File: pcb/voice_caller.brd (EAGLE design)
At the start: 22 parts, among them IC1 PRO_MICRO, IC2 AT45DB321D-S, IC3 78L12SMD, K4 G6J-2P-Y

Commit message: All but switches
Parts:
- added C7: (no value), rcl:C1206K
- moved C2 36.8 mm to (15.8, 39.8), turned to 0 degrees
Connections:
- net +3V3: now also C7.1
- net GND: now also C7.2
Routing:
- net GND: track 160.9 -> 164.2 mm
- net +5V: track 26.8 -> 29.9 mm
- net +3V3: track 10.2 -> 11.7 mm
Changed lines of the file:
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@@
 <elements>
 <element name="C1" library="rcl" package="C1206K" value="" x="37.823125" y="56.125625" rot="R180"/>
-<element name="C2" library="rcl" package="C1206K" value="" x="51.579403125" y="30.948178125" rot="R270"/>
+<element name="C2" library="rcl" package="C1206K" value="" x="15.803696875" y="39.752528125"/>
 <element name="IC2" library="memory-atmel" package="SO08-8S2" value="AT45DB321D-S" x="27.18" y="35.015" rot="R90"/>
 <element name="CONN_MIC" library="con-tycoelectronics" package="RJ45-NO-SHIELD" value="RJ45-8L-B" x="16.19" y="55.19" rot="R270">
@@
 <element name="R6" library="rcl" package="M1206" value="" x="36.37" y="9.68375" rot="R270"/>
 <element name="R7" library="rcl" package="M1206" value="1k" x="33.3375" y="23.65375" rot="R180"/>
+<element name="C7" library="rcl" package="C1206K" value="" x="19.446875" y="35.004375" rot="R270"/>
 </elements>
 <signals>
@@
 <wire x1="30.6775" y1="52.22875" x2="30.8375" y2="52.38875" width="0.3048" layer="1"/>
 <contactref element="K4" pad="1"/>
-<wire x1="35.123125" y1="52.79" x2="51.579403125" y2="32.448178125" width="0" layer="19" extent="1-1"/>
-<wire x1="29.781375" y1="16.66280625" x2="51.579403125" y2="32.448178125" width="0" layer="19" extent="1-1"/>
+<wire x1="14.303696875" y1="39.752528125" x2="14.5" y2="39.752528125" width="0.4064" layer="1"/>
+<wire x1="14.5" y1="39.752528125" x2="14.5" y2="42.62" width="0.4064" layer="1"/>
+<wire x1="29.781375" y1="16.66280625" x2="14.5" y2="39.752528125" width="0" layer="19" extent="1-1"/>
 </signal>
 <signal name="GND">
@@
 <wire x1="45.4025" y1="25.003125" x2="45.4025" y2="31.123125" width="0.3048" layer="1"/>
 <wire x1="45.4025" y1="31.123125" x2="45.47375" y2="31.194375" width="0.3048" layer="1"/>
+<contactref element="C7" pad="2"/>
+<wire x1="17.303696875" y1="39.752528125" x2="17.04" y2="39.752528125" width="0.4064" layer="1"/>
+<wire x1="17.04" y1="39.752528125" x2="17.04" y2="42.62" width="0.4064" layer="1"/>
 <wire x1="54.23255" y1="50.880025" x2="60.73495" y2="50.880025" width="0" layer="19" extent="1-1"/>
 <wire x1="40.323125" y1="51.52" x2="54.23255" y2="50.880025" width="0" layer="19" extent="1-1"/>
 <wire x1="19.58" y1="27.38" x2="18.811875" y2="24.685625" width="0" layer="19" extent="16-16"/>
-<wire x1="51.579403125" y1="29.448178125" x2="45.47375" y2="31.194375" width="0" layer="19" extent="1-1"/>
-<wire x1="55.36755" y1="29.588775" x2="51.579403125" y2="29.448178125" width="0" layer="19" extent="1-1"/>
+<wire x1="55.36755" y1="29.588775" x2="45.47375" y2="31.194375" width="0" layer="19" extent="1-1"/>
 <wire x1="61.86995" y1="29.588775" x2="55.36755" y2="29.588775" width="0" layer="19" extent="1-1"/>
+<wire x1="19.52625" y1="33.416875" x2="19.446875" y2="33.416875" width="0.4064" layer="1"/>
+<wire x1="19.446875" y1="33.416875" x2="19.446875" y2="33.504375" width="0.4064" layer="1"/>
 </signal>
 <signal name="MOSI">
@@
 <contactref element="IC1" pad="21"/>
 <contactref element="IC2" pad="6"/>
-<wire x1="23.455" y1="35.65" x2="21.261875" y2="35.65" width="0.3048" layer="1"/>
-<wire x1="21.261875" y1="35.65" x2="20.47875" y2="36.433125" width="0.3048" layer="1"/>
-<wire x1="20.47875" y1="36.433125" x2="20.47875" y2="38.655625" width="0.3048" layer="1"/>
+<wire x1="23.455" y1="35.65" x2="20.47875" y2="35.65" width="0.3048" layer="1"/>
+<wire x1="20.47875" y1="36.504375" x2="20.47875" y2="38.655625" width="0.3048" layer="1"/>
 <wire x1="20.47875" y1="38.655625" x2="22.145625" y2="40.3225" width="0.3048" layer="1"/>
 <wire x1="22.145625" y1="40.3225" x2="22.145625" y2="42.594375" width="0.3048" layer="1"/>
 <wire x1="22.145625" y1="42.594375" x2="22.12" y2="42.62" width="0.3048" layer="1"/>
+<contactref element="C7" pad="1"/>
+<wire x1="19.446875" y1="36.504375" x2="20.47875" y2="36.504375" width="0.3048" layer="1"/>
+<wire x1="20.47875" y1="35.65" x2="20.47875" y2="36.504375" width="0.3048" layer="1"/>
 </signal>
 <signal name="N$4">

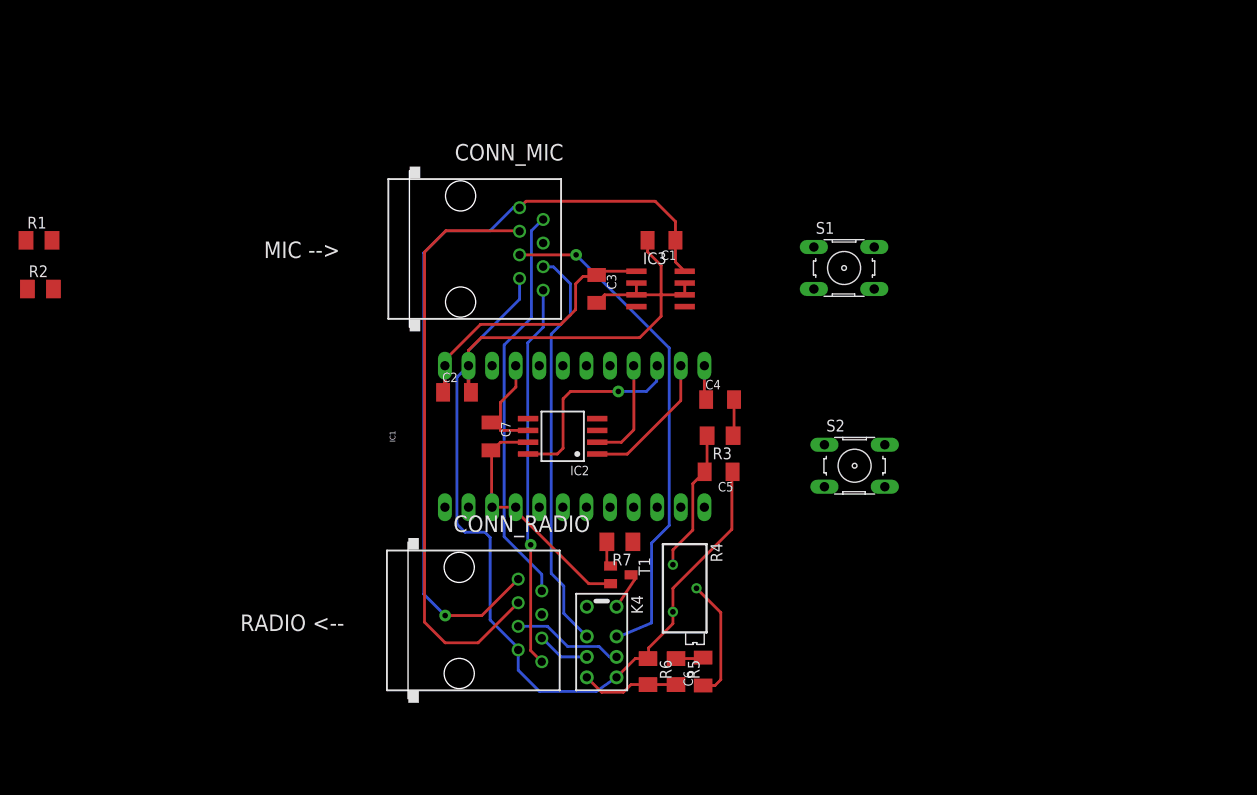
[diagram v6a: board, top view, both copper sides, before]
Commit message: Buttons and bistable relay added, PTT thing is missing.
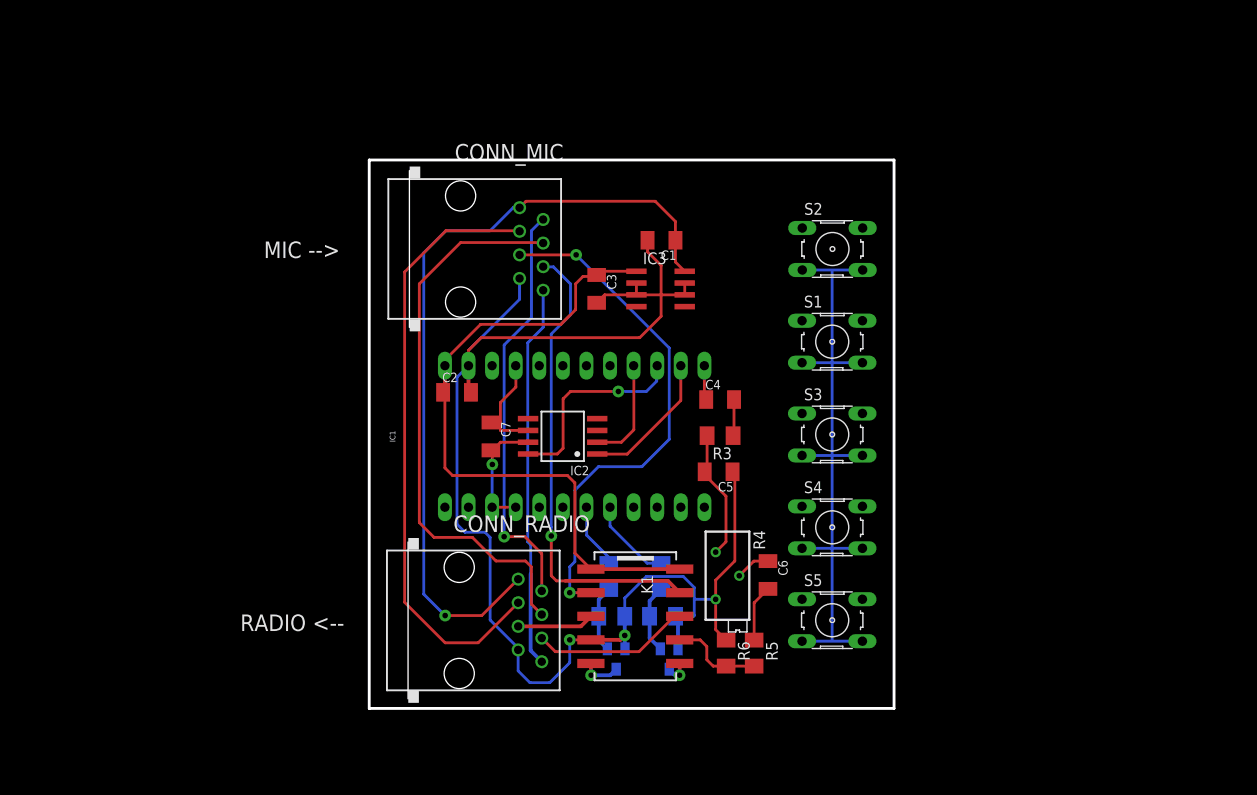
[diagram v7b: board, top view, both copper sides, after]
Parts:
- removed K4: G6J-2P-Y, relay:G6J-2P-Y
- removed R1: 3k9, rcl:M1206
- removed R2: 2k2, rcl:M1206
- removed R7: 1k, rcl:M1206
- removed T1: (no value), transistor:SOT23-BEC
- added K1: TQ2SA-L2-5V, relay:TQ-SA
- added R10, R8: 1k, rcl:M1206
- added R11, R9: 10k, rcl:M1206
- added S3, S4, S5: (no value), switch-omron:B3F-10XX
- added T2, T3: (no value), transistor:SOT23-BEC
- moved S2 23.5 mm to (56.2, 55.2)
- moved C6 12.5 mm to (49.3, 20.1), turned to 270 degrees
- moved R5 8.64 mm to (47.8, 11.7)
- moved R6 8.64 mm to (44.8, 11.7)
- moved S1 8.04 mm to (56.2, 45.2)
- moved R4 4.80 mm to (44.9, 20.0)
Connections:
- removed net DAH: R2.2
- removed net DIT: R1.2
- new net BUTTON1: S2.1
- new net BUTTON2: S1.1
- new net N$10: K1.5, T2.C
- new net N$11: R8.2, R9.2, T2.B
- new net N$12: S4.1
- new net N$13: K1.6, T3.C
- new net N$14: R10.2, R11.2, T3.B
- new net N$15: S5.1
- new net N$16: IC1.18
- new net N$17: IC1.17
- new net PULSE_RX: IC1.8, R10.1
- new net PULSE_TX: IC1.7, R8.1
- net +5V: now also K1.1, K1.10; no longer K4.1
- net FREQ_UD: no longer R1.1, R2.1
- net GND: now also K1.4, R11.1, R9.1, S3.3, S3.4, S4.3, S4.4, S5.3, S5.4, T2.E, T3.E; no longer K4.5, T1.E
- net MIC: now also K1.9; no longer K4.2
- net MIC_GND: now also K1.2; no longer K4.7
- net MIC_GND_RADIO: now also K1.3; no longer K4.6
- net MIC_PWM: now also K1.7; no longer K4.4
- net MIC_RADIO: now also K1.8; no longer K4.3
- net N$4: now also IC1.20; no longer K4.8, T1.C
- net N$5: now also IC1.19; no longer CONN_RADIO.4
- net N$9: now also S3.1; no longer R7.2, T1.B
- net PTT: now also CONN_RADIO.4
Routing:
- net GND: track 164.2 -> 243.7 mm, vias 0 -> 3
- net PTT: track 0.00 -> 60.5 mm
- net +5V: track 29.9 -> 72.2 mm
- net MIC_RADIO: track 5.69 -> 17.0 mm
- net N$6: track 13.1 -> 3.75 mm
- net PULSE_RX: track 0.00 -> 9.20 mm
- net N$14: track 0.00 -> 7.39 mm
- net N$11: track 0.00 -> 7.22 mm
- net PULSE_TX: track 0.00 -> 7.05 mm
- net MIC: track 44.1 -> 50.6 mm, vias 0 -> 1
- net N$10: track 0.00 -> 4.24 mm, vias 0 -> 1
- net N$4: track 4.22 -> 0.00 mm
- net MIC_GND_RADIO: track 12.0 -> 8.28 mm
- net N$3: track 2.96 -> 6.13 mm
- net N$9: track 2.77 -> 0.00 mm
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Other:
- board outline added: 56.5 x 59.1 mm
